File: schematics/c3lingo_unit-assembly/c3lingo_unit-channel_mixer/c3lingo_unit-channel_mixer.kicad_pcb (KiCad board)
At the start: 2 copper layers, 75 x 90 mm, 95 parts, among them J301 Interconnect, J303 I/O, Q301 MMBFJ113, SW301 OnAir_X, SW302 Mute_X, U301 TL072, U302 LM339, U303 LM339, U304 LM339, U305 LM833-N

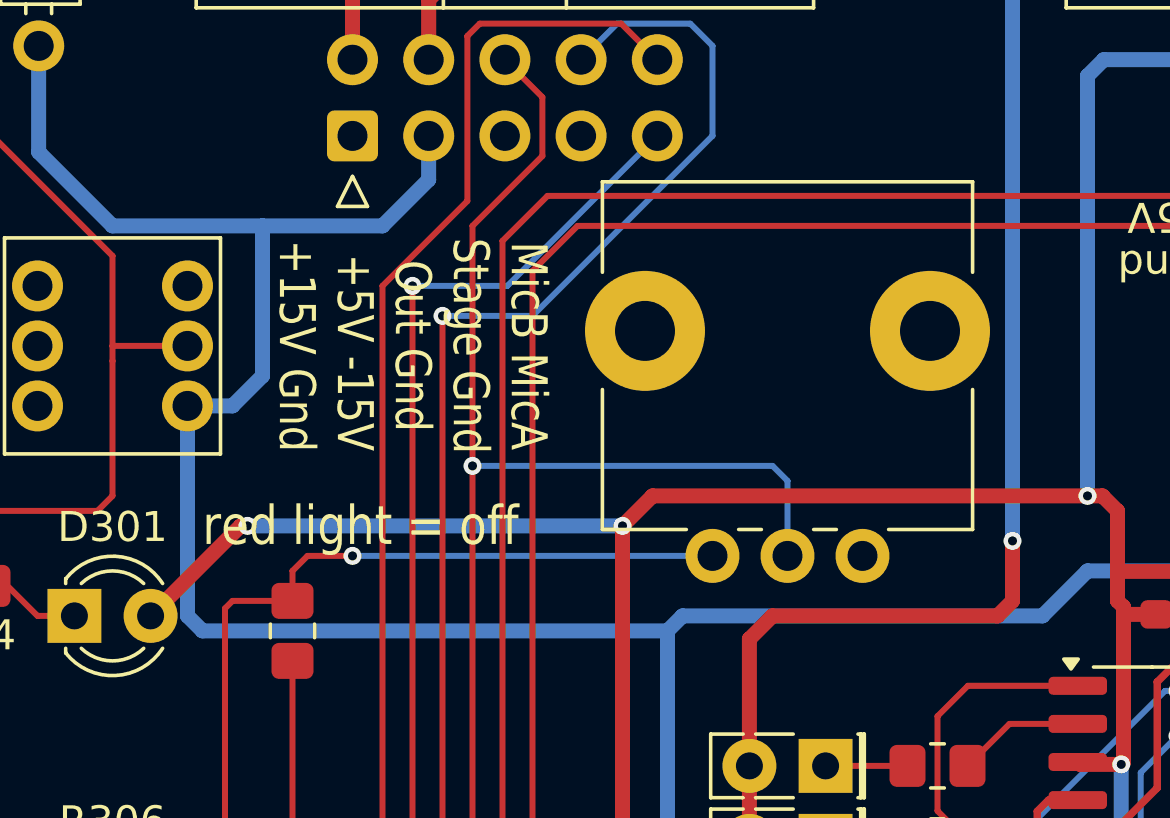
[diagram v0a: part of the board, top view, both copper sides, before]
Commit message: Channel-Mixer: Fix position of gain potentiometer
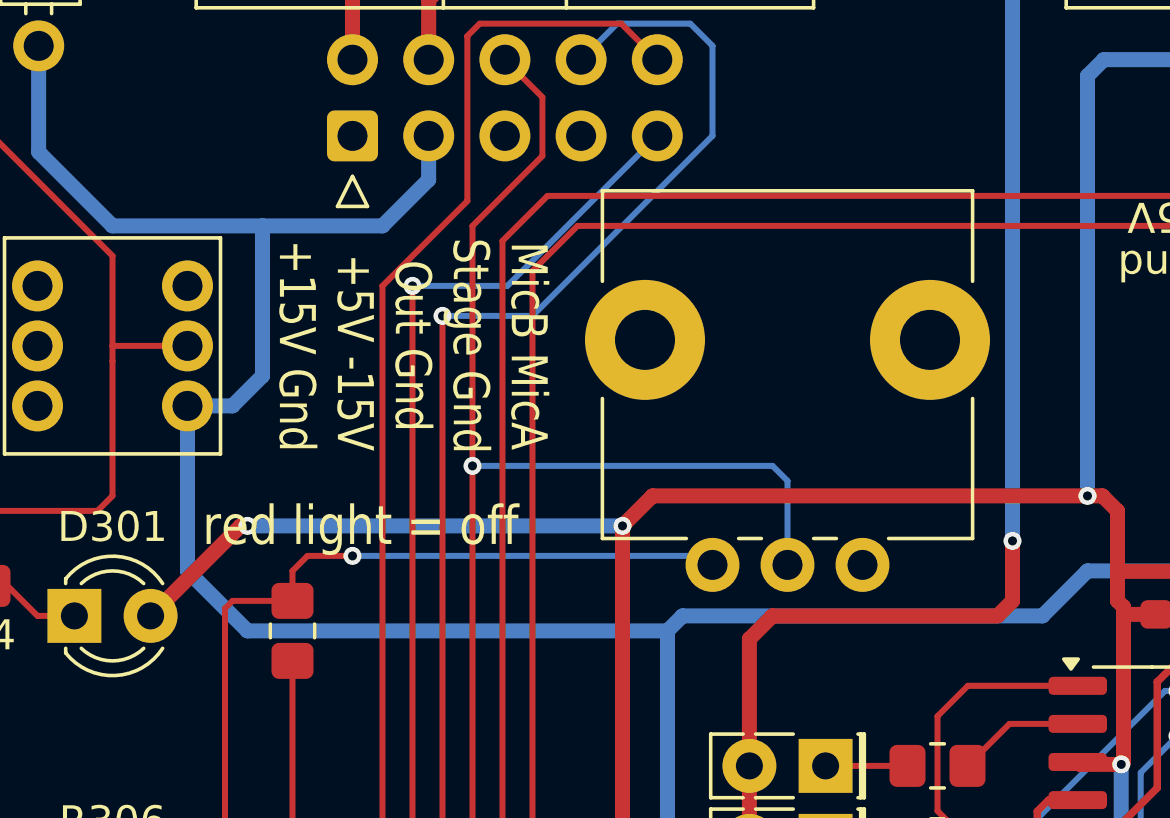
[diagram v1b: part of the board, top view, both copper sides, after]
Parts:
- moved RV302 0.30 mm to (87.5, 105.3)
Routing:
- net -15V: track 164.2 -> 163.3 mm
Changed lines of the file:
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@@
 	)
 	(footprint "c3lingo_unit-footprints:Potentiometer_CUI_PTN09X_Single_Vertical"
+		(locked yes)
 		(layer "F.Cu")
-		(at 87.5 105 90)
+		(at 87.5 105.3 90)
 		(descr "Potentiometer, vertical, Alps RK09L Double, http://www.alps.com/prod/info/E/HTML/Potentiometer/RotaryPotentiometers/RK09L/RK09L_list.html")
 		(tags "Potentiometer vertical Alps RK09L Double")
@@
 	(segment
 		(start 67.5 100)
-		(end 67.5 107)
+		(end 67.5 105.5)
 		(width 0.5)
 		(layer "B.Cu")
@@
 	)
 	(segment
-		(start 83.5 107.5)
-		(end 68 107.5)
-		(width 0.5)
-		(layer "B.Cu")
-		(net 1)
-	)
-	(segment
 		(start 65 94)
 		(end 62.54 91.54)
@@
 	)
 	(segment
-		(start 67.5 107)
-		(end 68 107.5)
+		(start 104.54 104.96)
+		(end 104 105.5)
 		(width 0.5)
 		(layer "B.Cu")
@@
 	)
 	(segment
-		(start 104.54 104.96)
+		(start 101.5 105.5)
 		(end 104 105.5)
 		(width 0.5)
@@
 	)
 	(segment
-		(start 101.5 105.5)
-		(end 104 105.5)
+		(start 83.5 107.5)
+		(end 69.5 107.5)
 		(width 0.5)
 		(layer "B.Cu")
@@
 		(width 0.5)
 		(layer "B.Cu")
+		(net 1)
+	)
+	(segment
+		(start 67.5 105.5)
+		(end 69.5 107.5)
+		(width 0.5)
+		(layer "B.Cu")

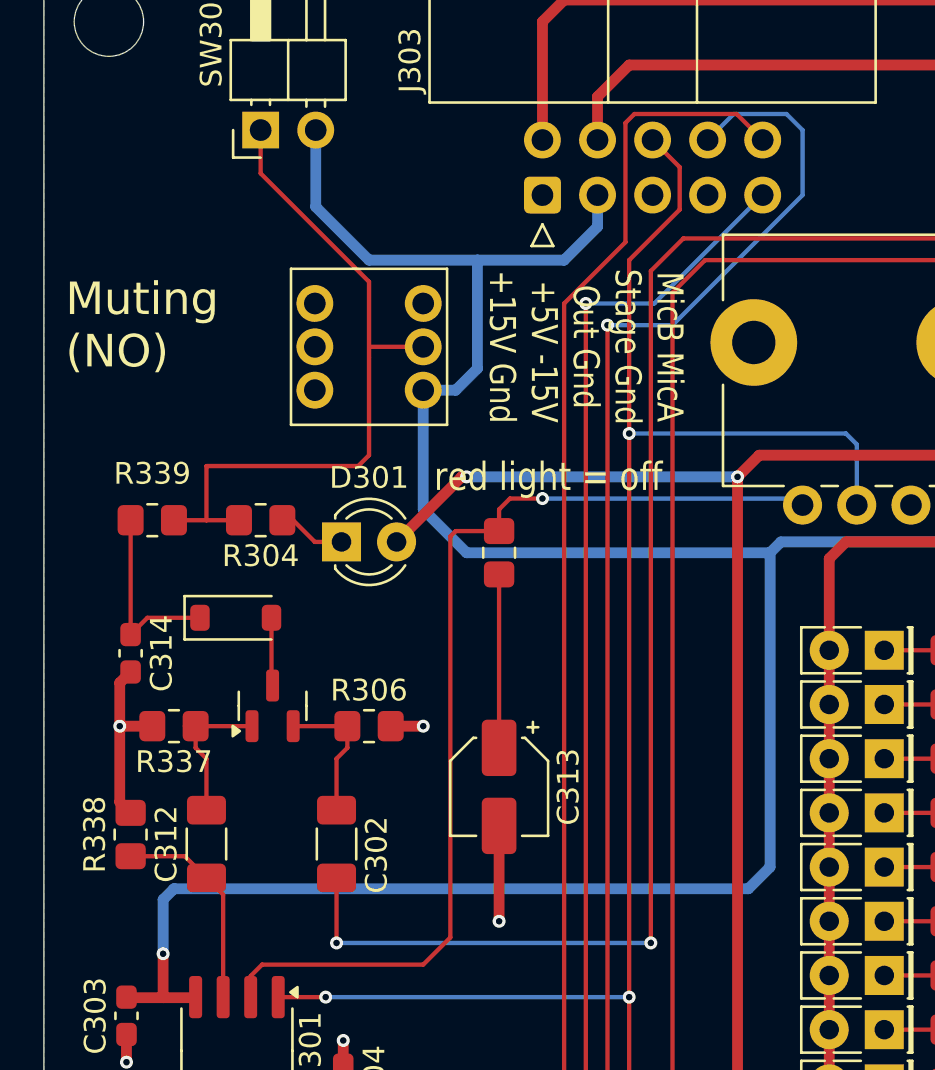
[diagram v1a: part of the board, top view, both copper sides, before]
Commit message: Channel-Mixer: Invert mute LED logic (to be an on-air LED)
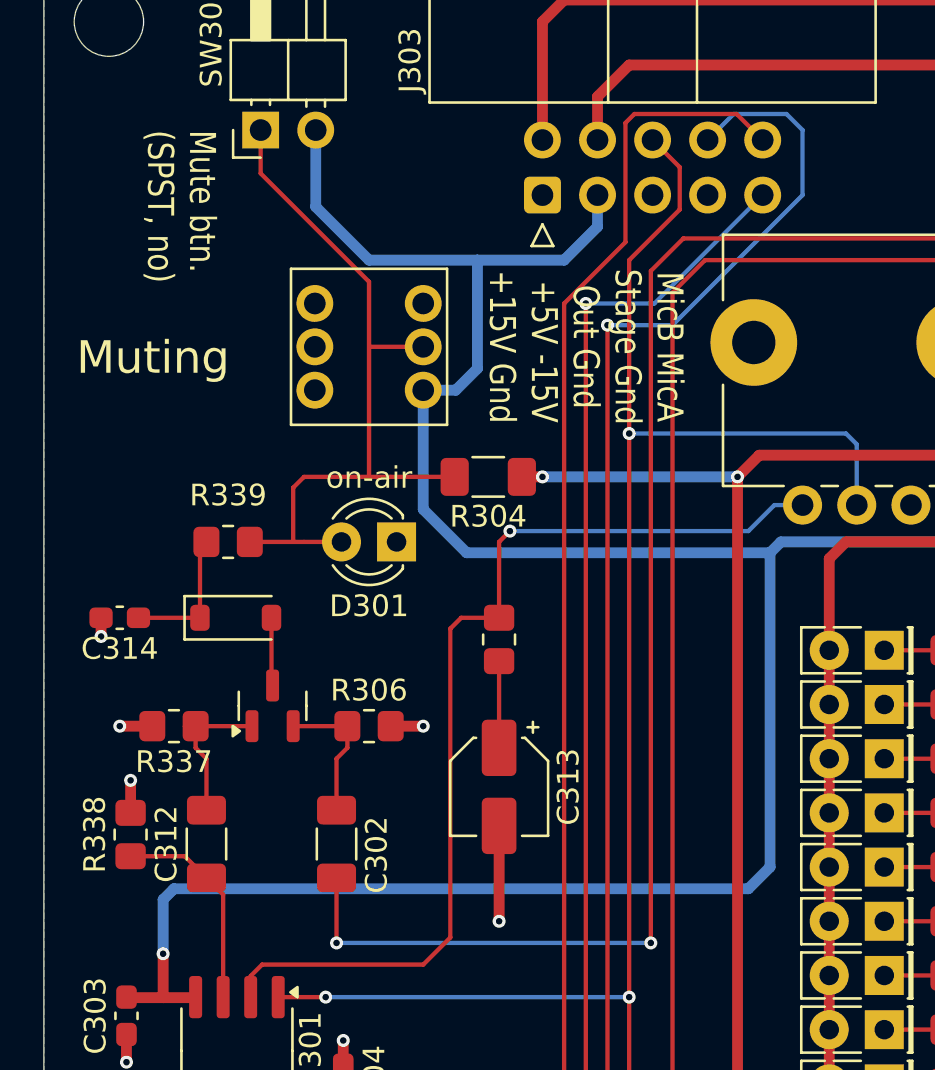
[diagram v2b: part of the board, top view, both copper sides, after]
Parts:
- D301: value muted (rd) -> on-air
- R304: value 10K -> 1K, 0.25W; footprint Resistor_SMD:R_0805_2012Metric_Pad1.20x1.40mm_HandSolder -> Resistor_SMD:R_1206_3216Metric_Pad1.30x1.75mm_HandSolder
- moved R304 10.7 mm to (70.5, 104.0)
- moved R303 4.00 mm to (71.0, 111.5)
- moved R339 3.64 mm to (58.5, 107.0)
- moved D301 2.54 mm to (66.3, 107.0), turned to 180 degrees
- moved C314 1.71 mm to (53.5, 110.5), turned to 180 degrees
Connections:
- D301 pad 1: Net-(D301-K) -> GND
- D301 pad 2: +15V -> Net-(D301-A)
- R304 pad 1: Net-(D301-K) -> +15V
- R304 pad 2: Net-(SW301A-B) -> Net-(D301-A)
- R339 pad 2: Net-(SW301A-B) -> Net-(D301-A)
- SW301 pad 2: Net-(SW301A-B) -> Net-(D301-A)
- SW302 pad 1: Net-(SW301A-B) -> Net-(D301-A)
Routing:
- net Net-(D301-A): track 0.00 -> 34.5 mm
- net Net-(SW301A-B): track 32.8 -> 0.00 mm
- net +15V: track 235.7 -> 228.7 mm
- net GND: track 35.3 -> 30.8 mm, vias 17 -> 19
- net Net-(D301-K): track 3.14 -> 0.00 mm
- net Net-(C313-Pad1): track 7.00 -> 4.00 mm
- net Net-(D316-K): track 8.80 -> 6.46 mm
- net Net-(U301A--): track 48.1 -> 46.9 mm
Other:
- board text added: "Mute btn. (SPST, no)"
- board text added: "Muting"
- board text added: "c3lingo Interpreter Unit Channel Mixer v0.5.0-dev 2024-09-28"
- board text removed: "Muting (NO)"
- board text removed: "c3lingo Interpreter Unit Channel Mixer v0.5.0-dev 2024-09-19"
- board text removed: "red light = off"

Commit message: Channel-Mixer: Add buffer cap for VU meter LEDs
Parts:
- added C315: 100nF, Capacitor_SMD:C_0603_1608Metric_Pad1.08x0.95mm_HandSolder, F.Cu at (88.1, 109.0)
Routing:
- net +5V: track 97.3 -> 98.3 mm
- net GND: track 30.8 -> 31.8 mm, vias 19 -> 20

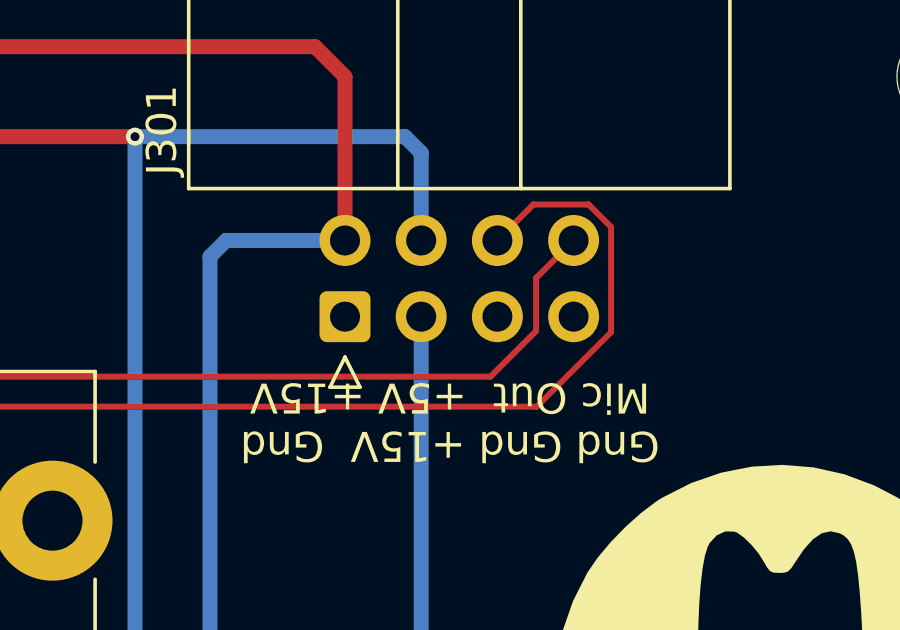
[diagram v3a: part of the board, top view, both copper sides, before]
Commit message: Channel: Swap mic and headphone signal on IDC connector
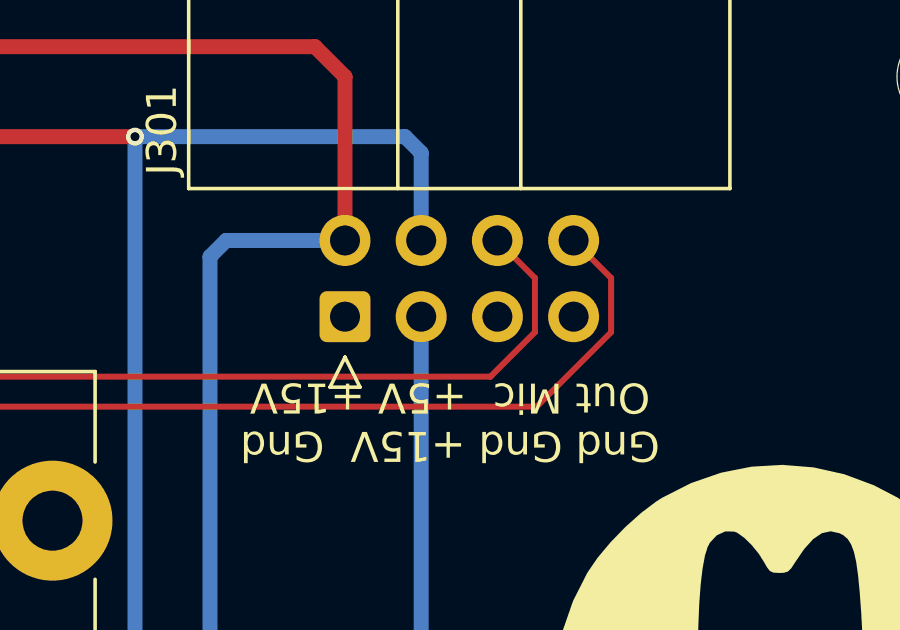
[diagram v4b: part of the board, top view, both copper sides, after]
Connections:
- J301 pad 6: /Headphone -> /MicPre
- J301 pad 8: /MicPre -> /Headphone
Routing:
- net /Headphone: track 109.9 -> 105.4 mm
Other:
- board text added: "Gnd Gnd +15V Gnd Out Mic +5V +15V"
- board text added: "c3lingo Interpreter Unit Channel Mixer v0.5.0-dev 2024-09-29"
- board text removed: "Gnd Gnd +15V Gnd Mic Out +5V +15V"
- board text removed: "c3lingo Interpreter Unit Channel Mixer v0.5.0-dev 2024-09-28"
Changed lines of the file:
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@@
 	(title_block
 		(title "c3lingo interpeter unit -- channel mixer")
-		(date "2025-09-28")
+		(date "2025-09-29")
 		(rev "v0.5.0-dev")
 		(company "Jannik Beyerstedt (jtbx)")
@@
 			(layers "*.Cu" "*.Mask")
 			(remove_unused_layers no)
-			(net 51 "/Headphone")
+			(net 52 "/MicPre")
 			(pinfunction "Pin_6")
 			(pintype "passive")
@@
 			(layers "*.Cu" "*.Mask")
 			(remove_unused_layers no)
-			(net 52 "/MicPre")
+			(net 51 "/Headphone")
 			(pinfunction "Pin_8")
 			(pintype "passive")
@@
 		)
 	)
-	(gr_text "Gnd Gnd +15V  Gnd\nMic Out  +5V +15V"
+	(gr_text "Gnd Gnd +15V  Gnd\nOut Mic  +5V +15V"
 		(at 105.5 94.5 180)
 		(layer "F.SilkS")
@@
 		)
 	)
-	(gr_text "c3lingo Interpreter Unit\nChannel Mixer\nv0.5.0-dev 2024-09-28"
+	(gr_text "c3lingo Interpreter Unit\nChannel Mixer\nv0.5.0-dev 2024-09-29"
 		(at 87.5 148 0)
 		(layer "B.SilkS")
@@
 	)
 	(segment
-		(start 110.117471 87.259)
-		(end 110.871 88.012529)
-		(width 0.2)
-		(layer "F.Cu")
-		(net 51)
-	)
-	(segment
-		(start 110.871 88.012529)
-		(end 110.871 91.518182)
-		(width 0.2)
-		(layer "F.Cu")
-		(net 51)
-	)
-	(segment
 		(start 60.225 138.275)
 		(end 60.5 138)
@@
 	)
 	(segment
-		(start 107.08 88.46)
-		(end 108.281 87.259)
+		(start 109.62 88.46)
+		(end 110.871 89.711)
 		(width 0.2)
 		(layer "F.Cu")
@@
 	)
 	(segment
+		(start 110.871 89.711)
+		(end 110.871 91.518182)
+		(width 0.2)
+		(layer "F.Cu")
+		(net 51)
+	)
+	(segment
 		(start 59.54 137.04)
 		(end 60.5 138)
@@
 	)
 	(segment
-		(start 108.281 87.259)
-		(end 110.117471 87.259)
-		(width 0.2)
-		(layer "F.Cu")
-		(net 51)
-	)
-	(segment
 		(start 110.871 91.518182)
 		(end 108.389182 94)
@@
 	)
 	(segment
-		(start 63.5 125.5)
-		(end 63.5 122.5)
+		(start 108.331 89.711)
+		(end 108.331 91.518182)
 		(width 0.2)
 		(layer "F.Cu")
@@
 	)
 	(segment
-		(start 106.849182 93)
-		(end 79.5 93)
+		(start 63.5 125.5)
+		(end 63.5 122.5)
 		(width 0.2)
 		(layer "F.Cu")
@@
 	)
 	(segment
-		(start 109.62 88.46)
-		(end 108.369 89.711)
+		(start 106.849182 93)
+		(end 79.5 93)
 		(width 0.2)
 		(layer "F.Cu")
@@
 	)
 	(segment
-		(start 108.369 89.711)
-		(end 108.369 91.480182)
+		(start 108.331 91.518182)
+		(end 106.849182 93)
 		(width 0.2)
 		(layer "F.Cu")
@@
 	)
 	(segment
-		(start 108.369 91.480182)
-		(end 106.849182 93)
+		(start 107.08 88.46)
+		(end 108.331 89.711)
 		(width 0.2)
 		(layer "F.Cu")

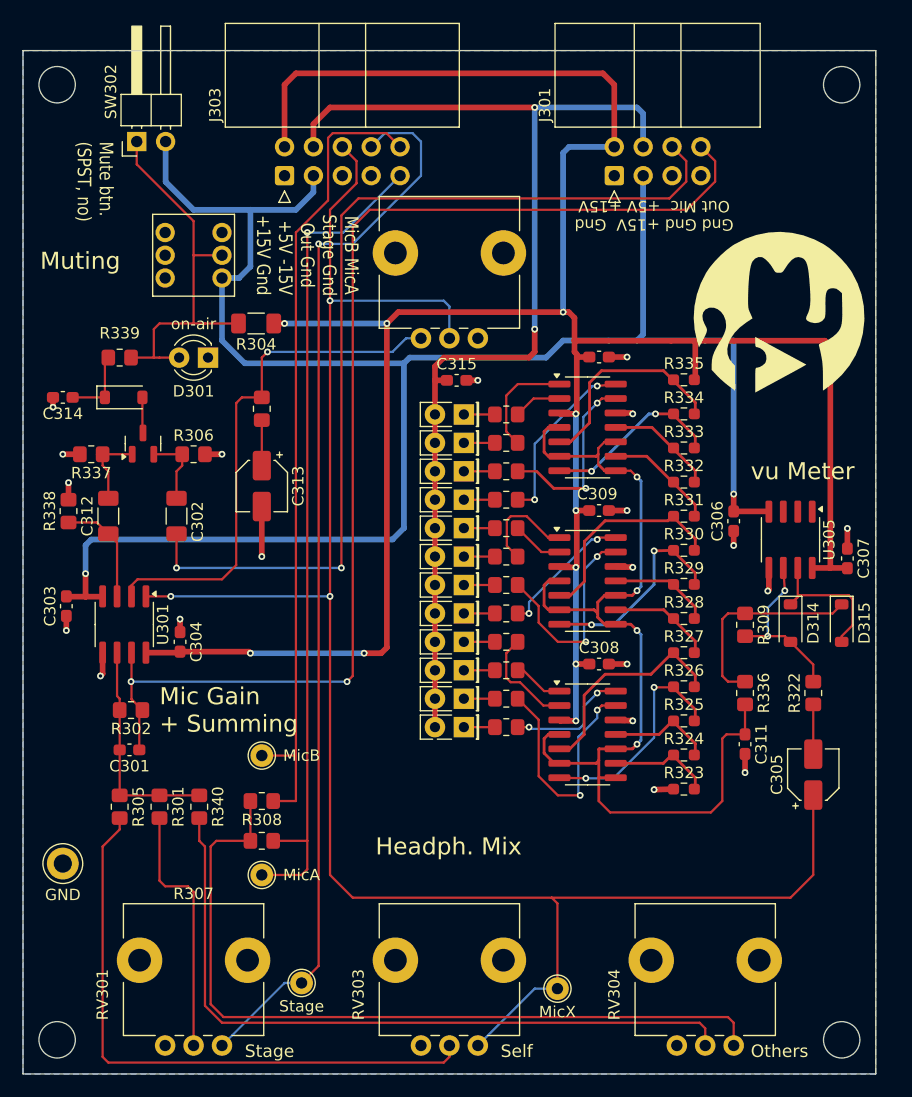
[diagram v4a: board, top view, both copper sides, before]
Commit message: Add some artwork to the PCBs
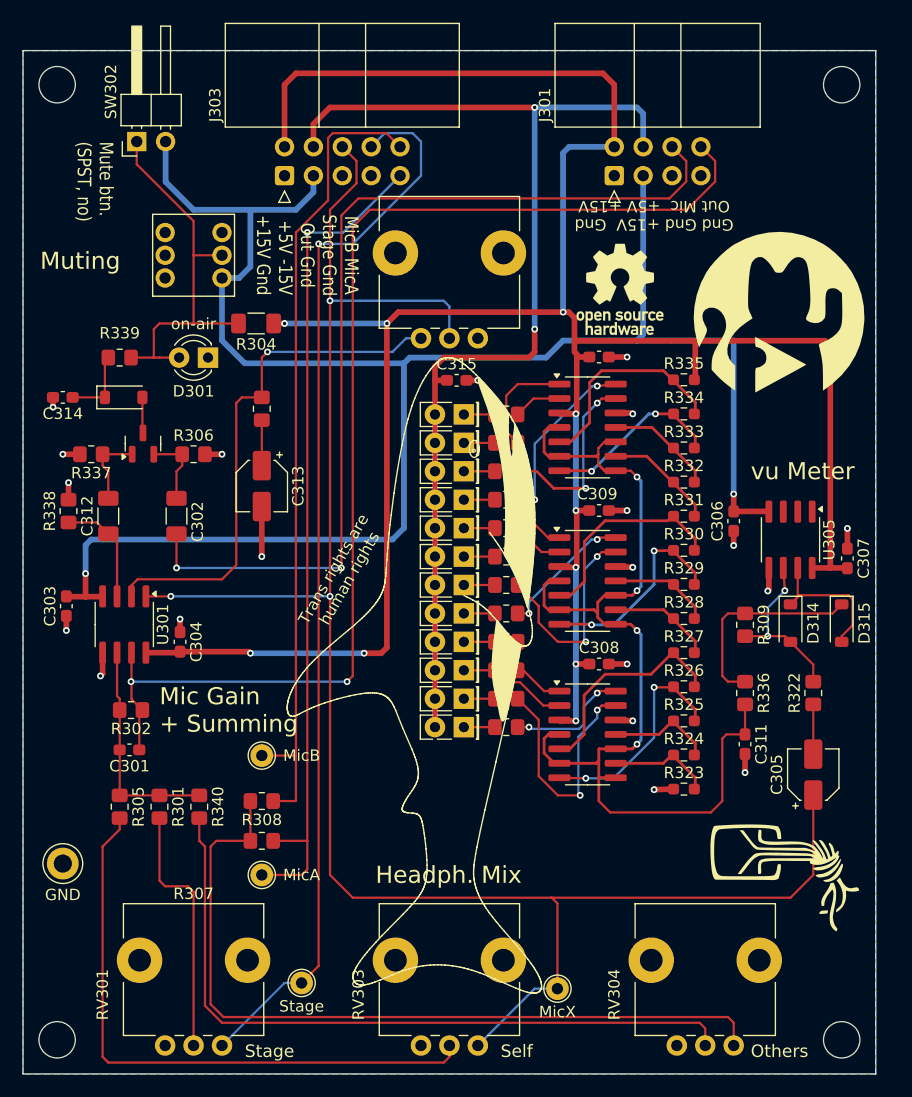
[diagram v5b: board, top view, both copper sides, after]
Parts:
- added G***: LOGO, c3lingo_unit-footprints:chaosknoten-10mm, F.Cu at (117.0, 152.5)
- added G***: LOGO, c3lingo_unit-footprints:antifa-15mm, B.Cu at (108.1, 127.0)
- added G***: LOGO, c3lingo_unit-footprints:chaosknoten-15mm, B.Cu at (67.5, 124.0)
- added REF**: OSHW-Logo_7.5x8mm_SilkScreen, Symbol:OSHW-Logo_7.5x8mm_SilkScreen, F.Cu at (102.5, 101.0)
- added REF**: Smolhaj_Scale_0.1, Symbol:Smolhaj_Scale_0.1, F.Cu at (87.5, 107.0)
- added REF**: Smolhaj_Scale_0.1, Symbol:Smolhaj_Scale_0.1, B.Cu at (58.5, 107.0)
- added REF**: OSHW-Logo_11.4x12mm_SilkScreen, Symbol:OSHW-Logo_11.4x12mm_SilkScreen, B.Cu at (71.0, 133.0)
- moved G*** 32.0 mm to (87.5, 153.0)
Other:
- board text added: "Trans rights are human rights"
- board text added: "c3lingo Interpreter Unit Channel Mixer v1.0.0 2024-10-16"
- board text removed: "c3lingo Interpreter Unit Channel Mixer v0.5.0-dev 2024-09-29"
